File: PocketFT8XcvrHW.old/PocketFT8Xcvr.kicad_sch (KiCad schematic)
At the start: 54 parts, among them J1 HX8357D SPI, J2 22-23-2021, J3 GPS, J5 HX8357D 8-BIT, Q1 2N3904, Q2 2N3906, Q3 2N7000, Q4 2N7000, U1 MCP3422A1T-E/SN, U2 Si4735-D60-GU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

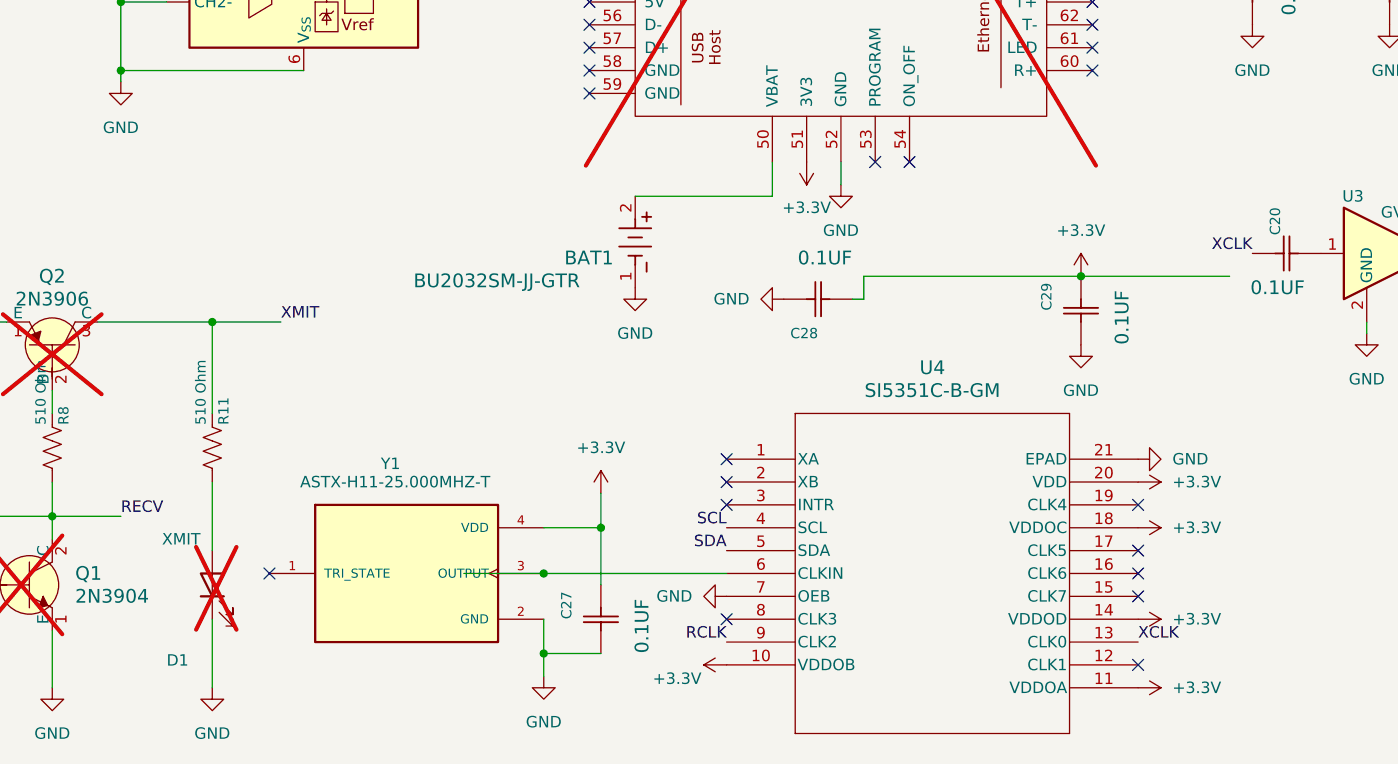
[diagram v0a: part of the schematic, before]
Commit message: Housecleaning after abandoning the QFN16 SI5351 package
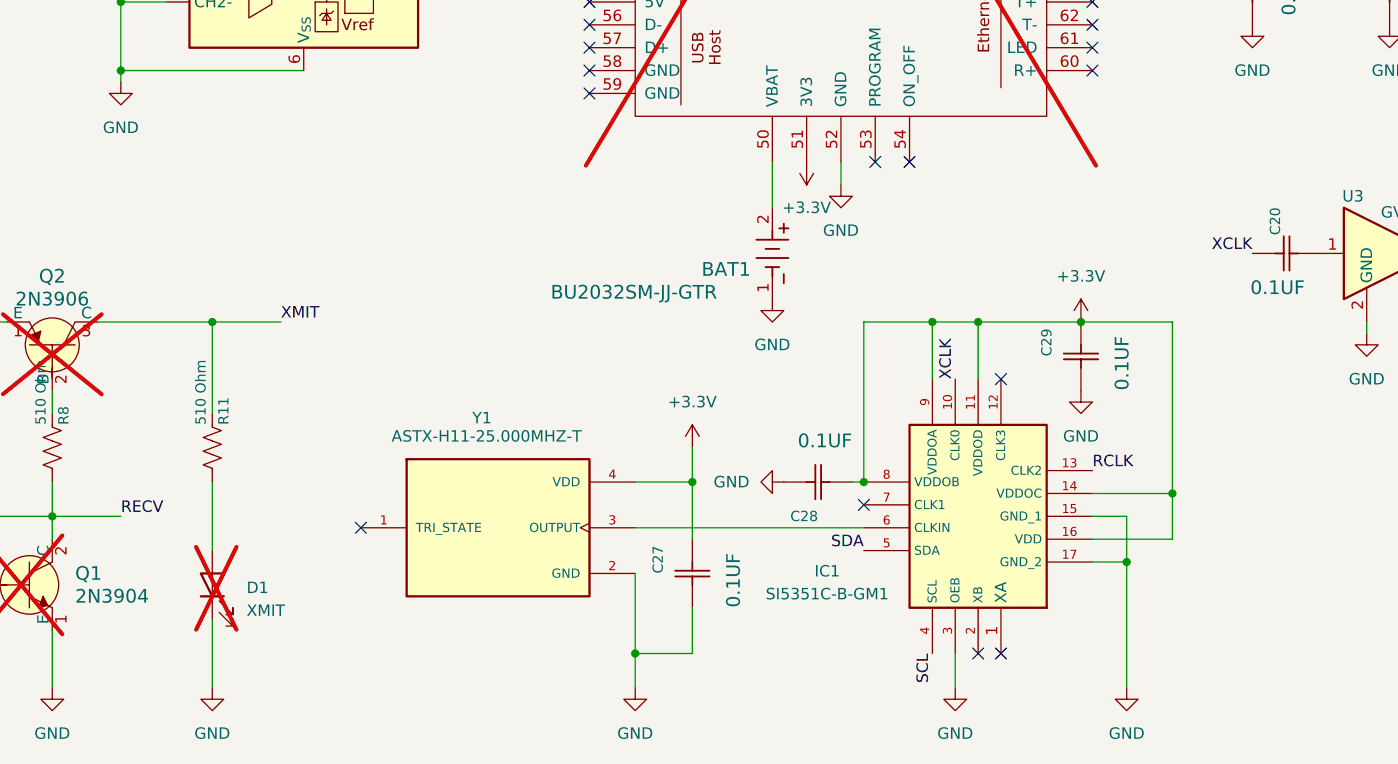
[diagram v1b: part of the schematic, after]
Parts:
- removed U4: SI5351C-B-GM, QFN20_4X4_SKY, symbol 2024-08-12_00-43-20:SI5351C-B-GM
- added IC1: SI5351C-B-GM1, SI5351C-B-GM1:QFN50P300X300X90-17N-D, symbol SI5351C-B-GM1:SI5351C-B-GM1
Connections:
- net +3.3V: now also IC1.11 (VDDOD), IC1.14 (VDDOC), IC1.16 (VDD), IC1.8 (VDDOB), IC1.9 (VDDOA)
- net GND: now also IC1.15 (GND_1), IC1.17 (GND_2), IC1.3 (OEB)
- net RCLK: now also IC1.13 (CLK2)
- net SCL: now also IC1.4 (SCL)
- net SDA: now also IC1.5 (SDA)
- net XCLK: now also IC1.10 (CLK0)
- net at Y1.3 (OUTPUT): now also IC1.6 (CLKIN)
- no-connect marks 83 -> 78
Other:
- moved on the sheet: BAT1, C27, C28, C29, Y1
